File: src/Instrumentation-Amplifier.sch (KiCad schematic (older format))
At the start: 9 parts, among them J1 PPTC041LFBN-RC, J2 PPTC041LFBN-RC, U1 LM7812_SMD, U2 AD623ARZ-R7

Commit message: Swapped 4 pin header component symbol
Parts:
- removed J1, J2: PPTC041LFBN-RC, Instrumentation-Amplifier:PPTC041LFBN-RC, symbol Instrumentation-Amplifier_L-0001:PPTC041LFBN-RC
- added P? (x2): 2043-1X04G00DAU, CONN_2043-1X04G00DAU_OUP, symbol Instrumentation-Amplifier_L-0001:2043-1X04G00DAU
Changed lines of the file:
@@
-$EndComp
-$Comp
-L Instrumentation-Amplifier_L-0001:PPTC041LFBN-RC J2
-U 1 1 60C4896D
-P 6400 5200
-F 0 "J2" V 6357 5430 50  0000 L CNN
-F 1 "PPTC041LFBN-RC" H 6070 5105 50  0001 R CNN
-F 2 "Instrumentation-Amplifier:PPTC041LFBN-RC" H 6900 4650 50  0001 L BNN
-F 3 "" H 6400 5200 50  0001 L BNN
-F 4 "" H 7250 4850 50  0001 L BNN "MAXIMUM_PACKAGE_HEIGHT"
-F 5 "" H 6400 5200 50  0001 L BNN "STANDARD"
-F 6 "" H 6400 5200 50  0001 L BNN "PARTREV"
-F 7 "" H 7250 4800 50  0001 L BNN "MANUFACTURER"
-	1    6400 5200
-	0    1    -1   0
 $EndComp
 $Comp
@@
 $EndComp
 $Comp
-L Instrumentation-Amplifier-rescue:Earth-power-Instrumentation-Amplifier-rescue #PWR02
+L Instrumentation-Amplifier_L-0001:Earth #PWR02
 U 1 1 60C7A04E
 P 4400 3900
@@
 	1    0    0    -1
 $EndComp
-$Comp
-L Instrumentation-Amplifier_L-0001:PPTC041LFBN-RC J1
-U 1 1 60C867DB
-P 2650 4100
-F 0 "J1" H 2607 4375 50  0000 C CNN
-F 1 "PPTC041LFBN-RC" H 2607 4376 50  0001 C CNN
-F 2 "Instrumentation-Amplifier:PPTC041LFBN-RC" H 3150 3550 50  0001 L BNN
-F 3 "" H 2650 4100 50  0001 L BNN
-	1    2650 4100
-	1    0    0    -1
-$EndComp
 Wire Wire Line
 	4400 3900 4400 3750
@@
 	4400 3750 4400 3650
 $Comp
-L Instrumentation-Amplifier-rescue:Earth-power-Instrumentation-Amplifier-rescue #PWR01
+L Instrumentation-Amplifier_L-0001:Earth #PWR01
 U 1 1 60CA2CA3
 P 3000 4500
@@
 	6400 4100 6800 4100
 $Comp
-L Instrumentation-Amplifier-rescue:Earth-power-Instrumentation-Amplifier-rescue #PWR04
+L Instrumentation-Amplifier_L-0001:Earth #PWR04
 U 1 1 60CD5E86
 P 6800 5000
@@
 Connection ~ 6800 4900
 $Comp
-L Instrumentation-Amplifier-rescue:Earth-power-Instrumentation-Amplifier-rescue #PWR05
+L Instrumentation-Amplifier_L-0001:Earth #PWR05
 U 1 1 60CED2BF
 P 8400 4500
@@
 	8400 4200 8650 4200
 $Comp
-L Instrumentation-Amplifier-rescue:Earth-power-Instrumentation-Amplifier-rescue #PWR06
+L Instrumentation-Amplifier_L-0001:Earth #PWR06
 U 1 1 60CF0331
 P 8650 4900
@@
 Connection ~ 5750 3150
 $Comp
-L Instrumentation-Amplifier-rescue:Earth-power-Instrumentation-Amplifier-rescue #PWR03
+L Instrumentation-Amplifier_L-0001:Earth #PWR03
 U 1 1 60D1305C
 P 5750 3800
@@
 Wire Wire Line
 	3000 4300 3000 4500
+$Comp
+L Instrumentation-Amplifier_L-0001:2043-1X04G00DAU P?
+U 1 1 6153D20A
+P 2850 4000
+F 0 "P?" H 3092 4181 60  0000 C CNN
+F 1 "2043-1X04G00DAU" H 3092 4181 60  0001 C CNN
+F 2 "CONN_2043-1X04G00DAU_OUP" H 3200 3450 60  0001 C CNN
+F 3 "" H 2850 4000 60  0000 C CNN
+	1    2850 4000
+	-1   0    0    -1
+$EndComp
+$Comp
+L Instrumentation-Amplifier_L-0001:2043-1X04G00DAU P?
+U 1 1 61541FED
+P 6500 5000
+F 0 "P?" V 6689 5128 60  0000 L CNN
+F 1 "2043-1X04G00DAU" V 6795 5128 60  0000 L CNN
+F 2 "CONN_2043-1X04G00DAU_OUP" H 6850 4450 60  0001 C CNN
+F 3 "" H 6500 5000 60  0000 C CNN
+	1    6500 5000
+	0    1    1    0
+$EndComp
 $EndSCHEMATC

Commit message: Updated schematic with global labels
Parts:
- gave numbers to parts that had none: 2
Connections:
- net labels added: VOUT
- net labels removed: Vo, Vout
- wire segments 40 -> 35
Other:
- note added: "Amplifier"
- note added: "Power Supply"
- moved on the sheet: C1, C2, D1, P1, P2, R1, R2, U1, U2

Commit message: Updated PCB with new connectors
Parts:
- P1, P2: footprint CONN_2043-1X04G00DAU_OUP -> Instrumentation-Amplifier:2043-1X04G00DAU
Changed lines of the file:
@@
 F 0 "P1" H 2342 4081 60  0000 C CNN
 F 1 "2043-1X04G00DAU" H 2342 4081 60  0001 C CNN
-F 2 "CONN_2043-1X04G00DAU_OUP" H 2450 3350 60  0001 C CNN
+F 2 "Instrumentation-Amplifier:2043-1X04G00DAU" H 2450 3350 60  0001 C CNN
 F 3 "" H 2100 3900 60  0000 C CNN
 	1    2100 3900
@@
 F 0 "P2" H 6842 4281 60  0000 C CNN
 F 1 "2043-1X04G00DAU" V 6895 4228 60  0001 L CNN
-F 2 "CONN_2043-1X04G00DAU_OUP" H 6950 3550 60  0001 C CNN
+F 2 "Instrumentation-Amplifier:2043-1X04G00DAU" H 6950 3550 60  0001 C CNN
 F 3 "" H 6600 4100 60  0000 C CNN
 	1    6600 4100

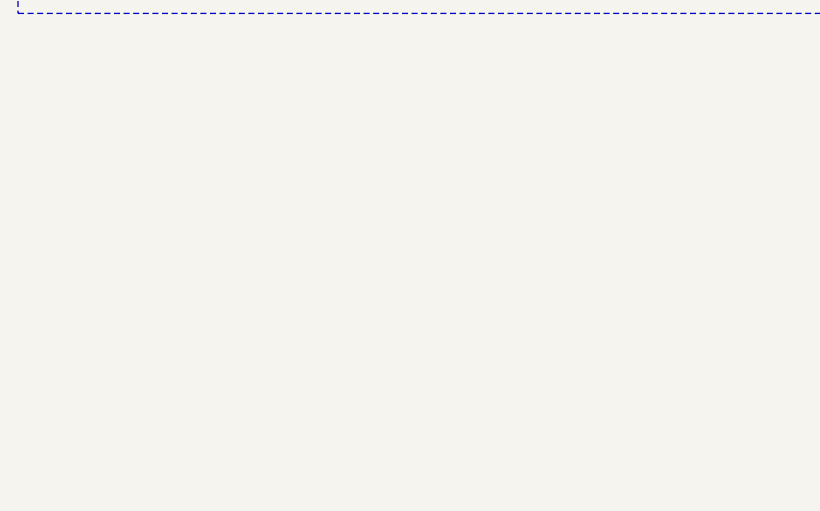
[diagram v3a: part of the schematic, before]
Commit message: Added mounting holes
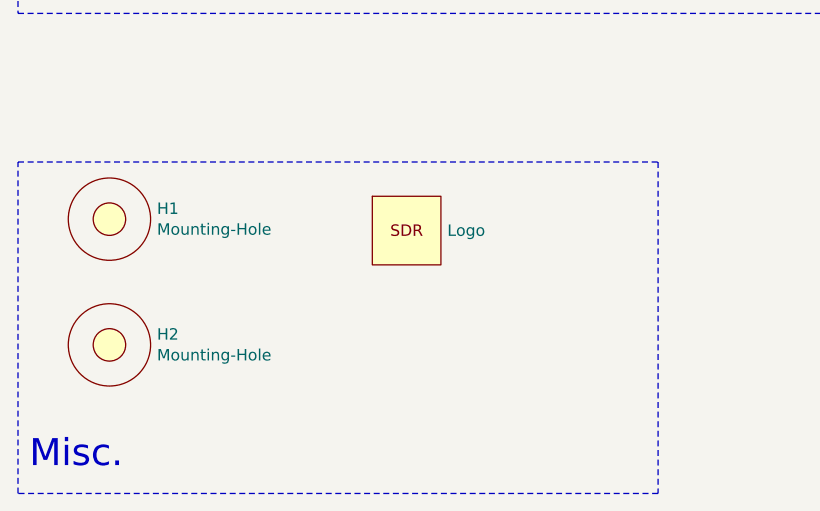
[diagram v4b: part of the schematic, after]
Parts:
- added H1, H2: Mounting-Hole, Instrumentation-Amplifier:MountingHole_2.1mm, symbol Instrumentation-Amplifier_L-0001:Mounting-Hole
- added LOGO1: Logo, Instrumentation-Amplifier:logo2, symbol Instrumentation-Amplifier_L-0001:Logo
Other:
- note added: "Misc."
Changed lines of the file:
@@
 Text Notes 5650 5000 0    118  ~ 0
 Amplifier
+$Comp
+L Instrumentation-Amplifier_L-0001:Mounting-Hole H1
+U 1 1 615380CC
+P 1750 6000
+F 0 "H1" H 1958 6046 50  0000 L CNN
+F 1 "Mounting-Hole" H 1958 5955 50  0000 L CNN
+F 2 "Instrumentation-Amplifier:MountingHole_2.1mm" H 1750 6000 50  0001 C CNN
+F 3 "" H 1750 6000 50  0001 C CNN
+	1    1750 6000
+	1    0    0    -1
+$EndComp
+$Comp
+L Instrumentation-Amplifier_L-0001:Mounting-Hole H2
+U 1 1 6153919E
+P 1750 6550
+F 0 "H2" H 1958 6596 50  0000 L CNN
+F 1 "Mounting-Hole" H 1958 6505 50  0000 L CNN
+F 2 "Instrumentation-Amplifier:MountingHole_2.1mm" H 1750 6550 50  0001 C CNN
+F 3 "" H 1750 6550 50  0001 C CNN
+	1    1750 6550
+	1    0    0    -1
+$EndComp
+Wire Notes Line
+	4150 5750 4150 7200
+Wire Notes Line
+	4150 7200 1350 7200
+Wire Notes Line
+	1350 7200 1350 5750
+Wire Notes Line
+	1350 5750 4150 5750
+Text Notes 1400 7100 0    118  ~ 0
+Misc.
+$Comp
+L Instrumentation-Amplifier_L-0001:Logo LOGO1
+U 1 1 615443B8
+P 3050 6050
+F 0 "LOGO1" H 3228 6096 50  0001 L CNN
+F 1 "Logo" H 3228 6050 50  0000 L CNN
+F 2 "Instrumentation-Amplifier:logo2" H 3050 6050 50  0001 C CNN
+F 3 "" H 3050 6050 50  0001 C CNN
+	1    3050 6050
+	1    0    0    -1
+$EndComp
 $EndSCHEMATC

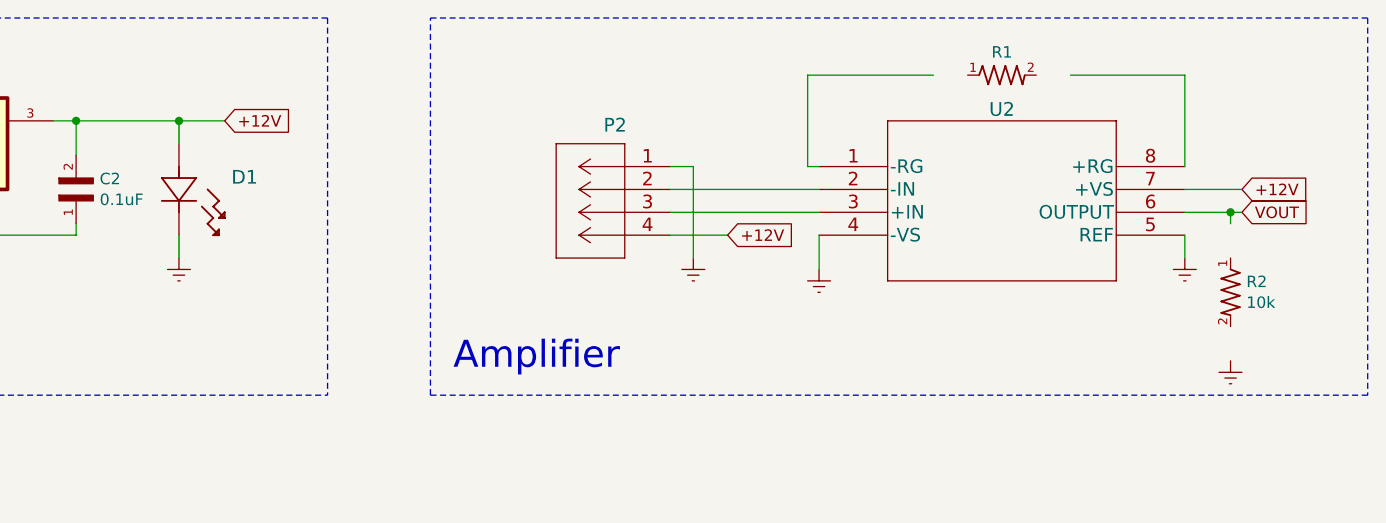
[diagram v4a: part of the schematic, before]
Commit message: Added LED resistor
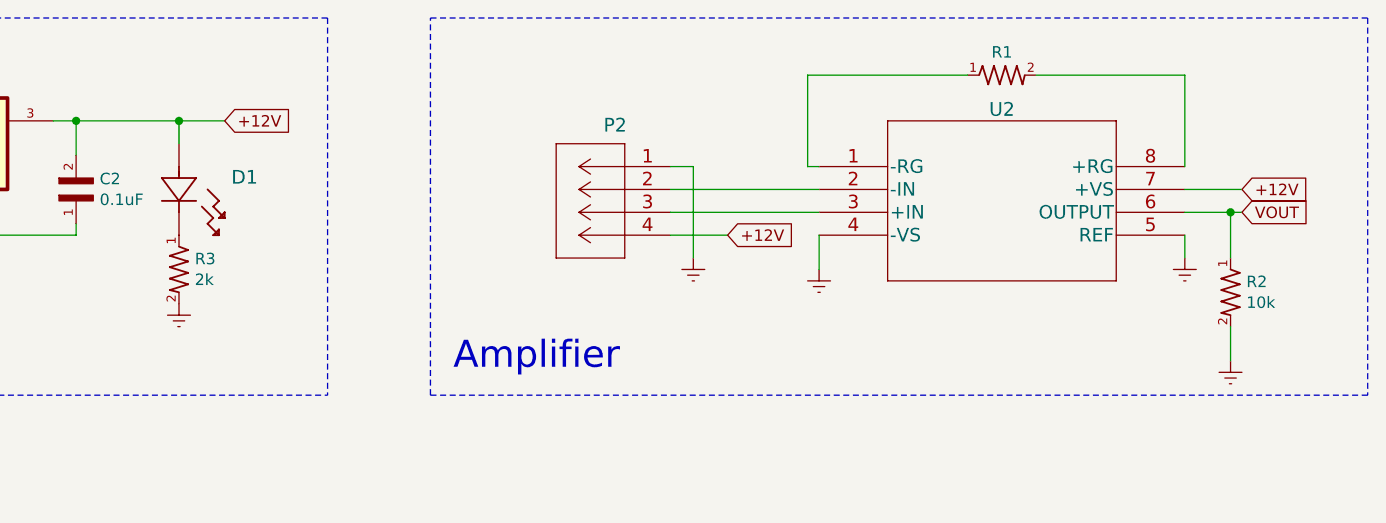
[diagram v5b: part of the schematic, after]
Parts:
- added R3: 2k, symbol Instrumentation-Amplifier_L-0001:RES_0603
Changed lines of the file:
@@
 	1    0    0    -1
 $EndComp
-Wire Wire Line
-	4450 4400 4450 4500
 $Comp
 L Instrumentation-Amplifier_L-0001:Earth #PWR03
 U 1 1 60D1305C
-P 4450 4500
-F 0 "#PWR03" H 4450 4250 50  0001 C CNN
-F 1 "Earth" H 4450 4350 50  0001 C CNN
-F 2 "" H 4450 4500 50  0001 C CNN
-F 3 "~" H 4450 4500 50  0001 C CNN
-	1    4450 4500
+P 4450 4700
+F 0 "#PWR03" H 4450 4450 50  0001 C CNN
+F 1 "Earth" H 4450 4550 50  0001 C CNN
+F 2 "" H 4450 4700 50  0001 C CNN
+F 3 "~" H 4450 4700 50  0001 C CNN
+	1    4450 4700
 	1    0    0    -1
 $EndComp
@@
 	7200 4100 7200 3700
 Wire Wire Line
-	7200 3700 7750 3700
-Wire Wire Line
-	8350 3700 8850 3700
-Wire Wire Line
 	8850 3700 8850 4100
 Wire Wire Line
@@
 Wire Wire Line
 	8850 4300 9050 4300
-Wire Wire Line
-	9050 4350 9050 4300
 Connection ~ 9050 4300
 Wire Wire Line
@@
 	1    0    0    -1
 $EndComp
+$Comp
+L Instrumentation-Amplifier_L-0001:RES_0603 R3
+U 1 1 615A3FED
+P 4450 4550
+F 0 "R3" V 4404 4619 50  0000 L CNN
+F 1 "2k" V 4495 4619 50  0000 L CNN
+F 2 "" H 4500 4050 50  0001 L BNN
+F 3 "" H 4450 4550 50  0001 L BNN
+	1    4450 4550
+	0    1    1    0
+$EndComp
+Wire Wire Line
+	8200 3700 8850 3700
+Wire Wire Line
+	7200 3700 7900 3700
+Wire Wire Line
+	9050 4300 9050 4500
+Wire Wire Line
+	9050 4950 9050 4800
 $EndSCHEMATC

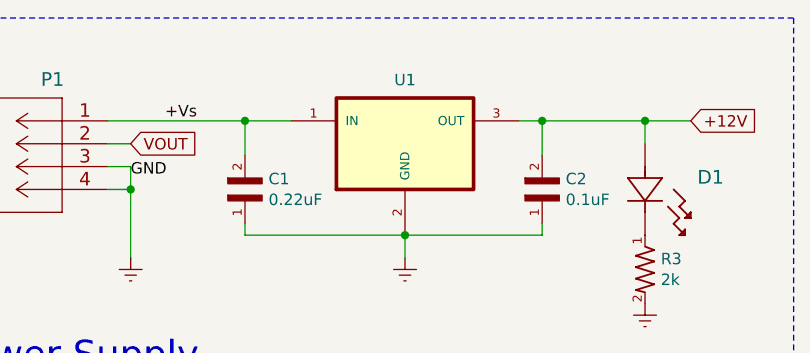
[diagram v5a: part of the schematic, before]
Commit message: Added new 3D view image
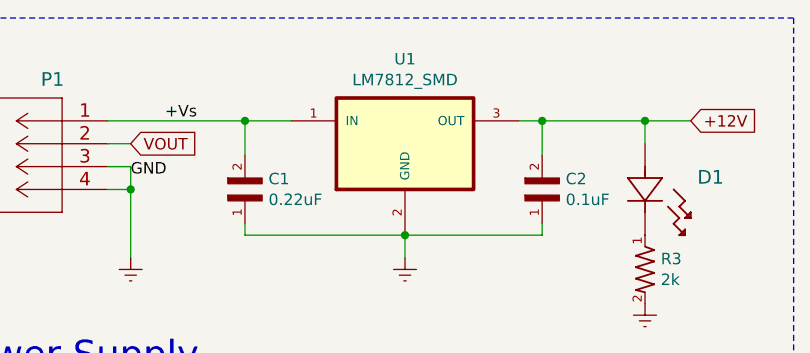
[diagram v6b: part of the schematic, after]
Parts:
- R3: footprint (none) -> Instrumentation-Amplifier:RES_0603
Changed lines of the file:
@@
 	4000 3900 4450 3900
 Connection ~ 4000 3900
-$Comp
-L Instrumentation-Amplifier_L-0001:LM7812_SMD U1
-U 1 1 60C7D957
-P 3400 4000
-F 0 "U1" H 3400 4279 50  0000 C CNN
-F 1 "LM7812_SMD" H 3400 4279 50  0001 C CNN
-F 2 "Instrumentation-Amplifier:LM7812" H 3550 3500 50  0001 L BNN
-F 3 "" H 3400 4000 50  0001 L BNN
-F 4 "IPC-7351B" H 3550 3600 50  0001 L BNN "STANDARD"
-F 5 "34" H 3650 3450 50  0001 L BNN "PARTREV"
-F 6 "STMicroelectronics" H 3550 3400 50  0001 L BNN "MANUFACTURER"
-	1    3400 4000
-	1    0    0    -1
-$EndComp
 Wire Wire Line
 	4000 4400 3400 4400
@@
 F 0 "R3" V 4404 4619 50  0000 L CNN
 F 1 "2k" V 4495 4619 50  0000 L CNN
-F 2 "" H 4500 4050 50  0001 L BNN
+F 2 "Instrumentation-Amplifier:RES_0603" H 4500 4050 50  0001 L BNN
 F 3 "" H 4450 4550 50  0001 L BNN
 	1    4450 4550
@@
 Wire Wire Line
 	9050 4950 9050 4800
+$Comp
+L Instrumentation-Amplifier_L-0001:LM7812_SMD U1
+U 1 1 615B2268
+P 3400 4000
+F 0 "U1" H 3400 4370 50  0000 C CNN
+F 1 "LM7812_SMD" H 3400 4279 50  0000 C CNN
+F 2 "Instrumentation-Amplifier:LM7812" H 3550 3500 50  0001 L BNN
+F 3 "" H 3400 4000 50  0001 L BNN
+F 4 "IPC-7351B" H 3550 3600 50  0001 L BNN "STANDARD"
+F 5 "34" H 3650 3450 50  0001 L BNN "PARTREV"
+F 6 "STMicroelectronics" H 3550 3400 50  0001 L BNN "MANUFACTURER"
+	1    3400 4000
+	1    0    0    -1
+$EndComp
 $EndSCHEMATC
